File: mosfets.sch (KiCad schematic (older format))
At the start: 28 parts, among them Q12 PSMN1R2-30YLC,115, Q13 PSMN1R2-30YLC,115, Q14 PSMN1R2-30YLC,115, Q15 IRLML0030TRPbF, Q16 IRLML0030TRPbF, Q17 IRLML0030TRPbF, Q18 IRLML0030TRPbF

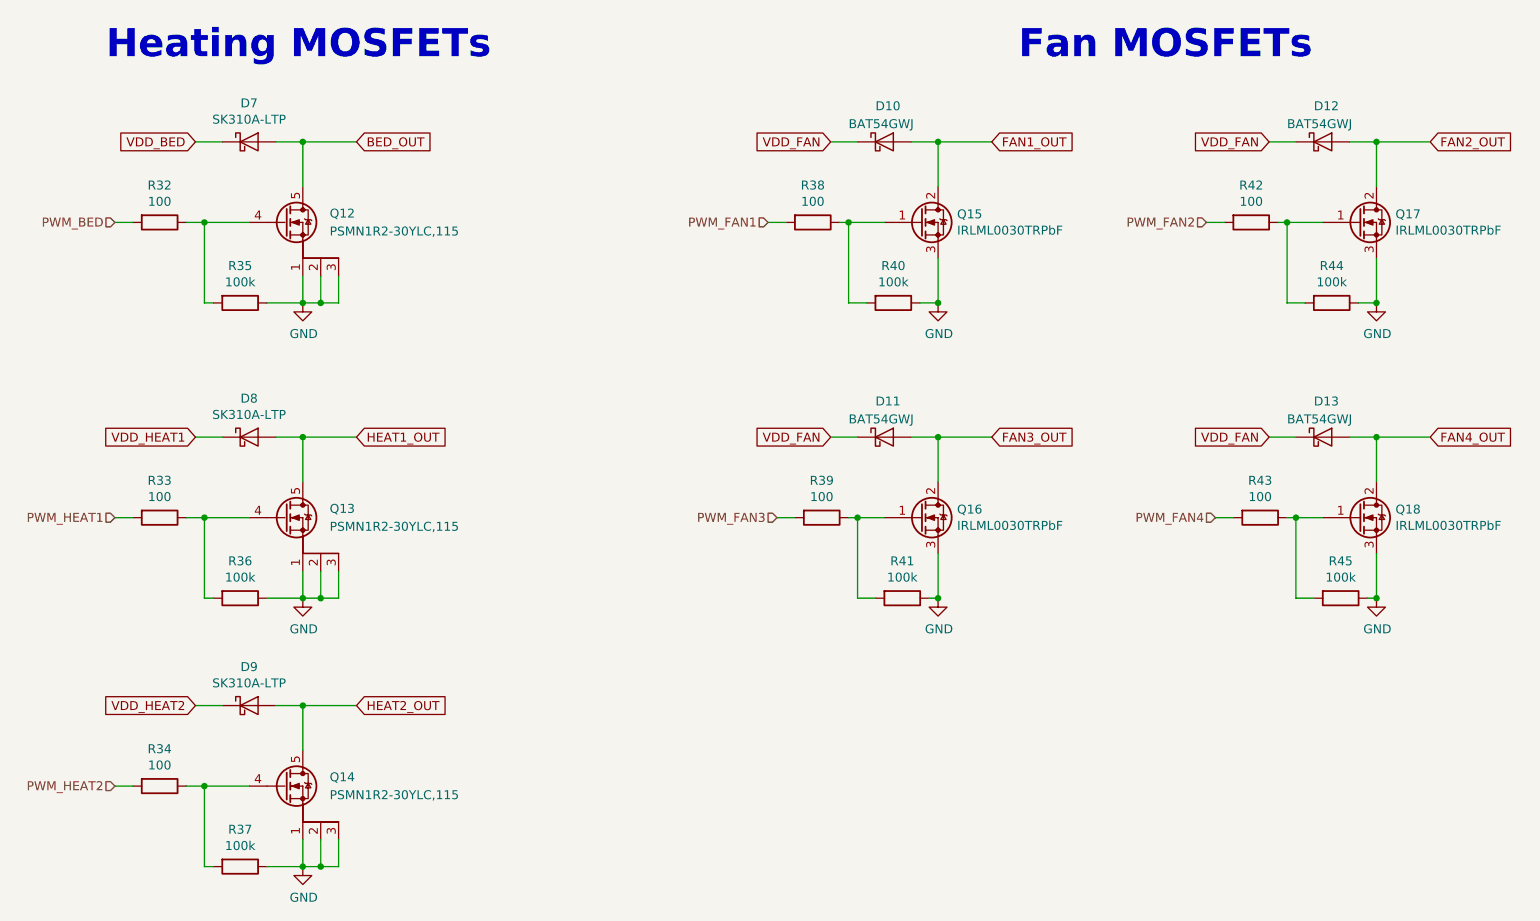
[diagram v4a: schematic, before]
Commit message: Add PD resistor to BOOT PIN
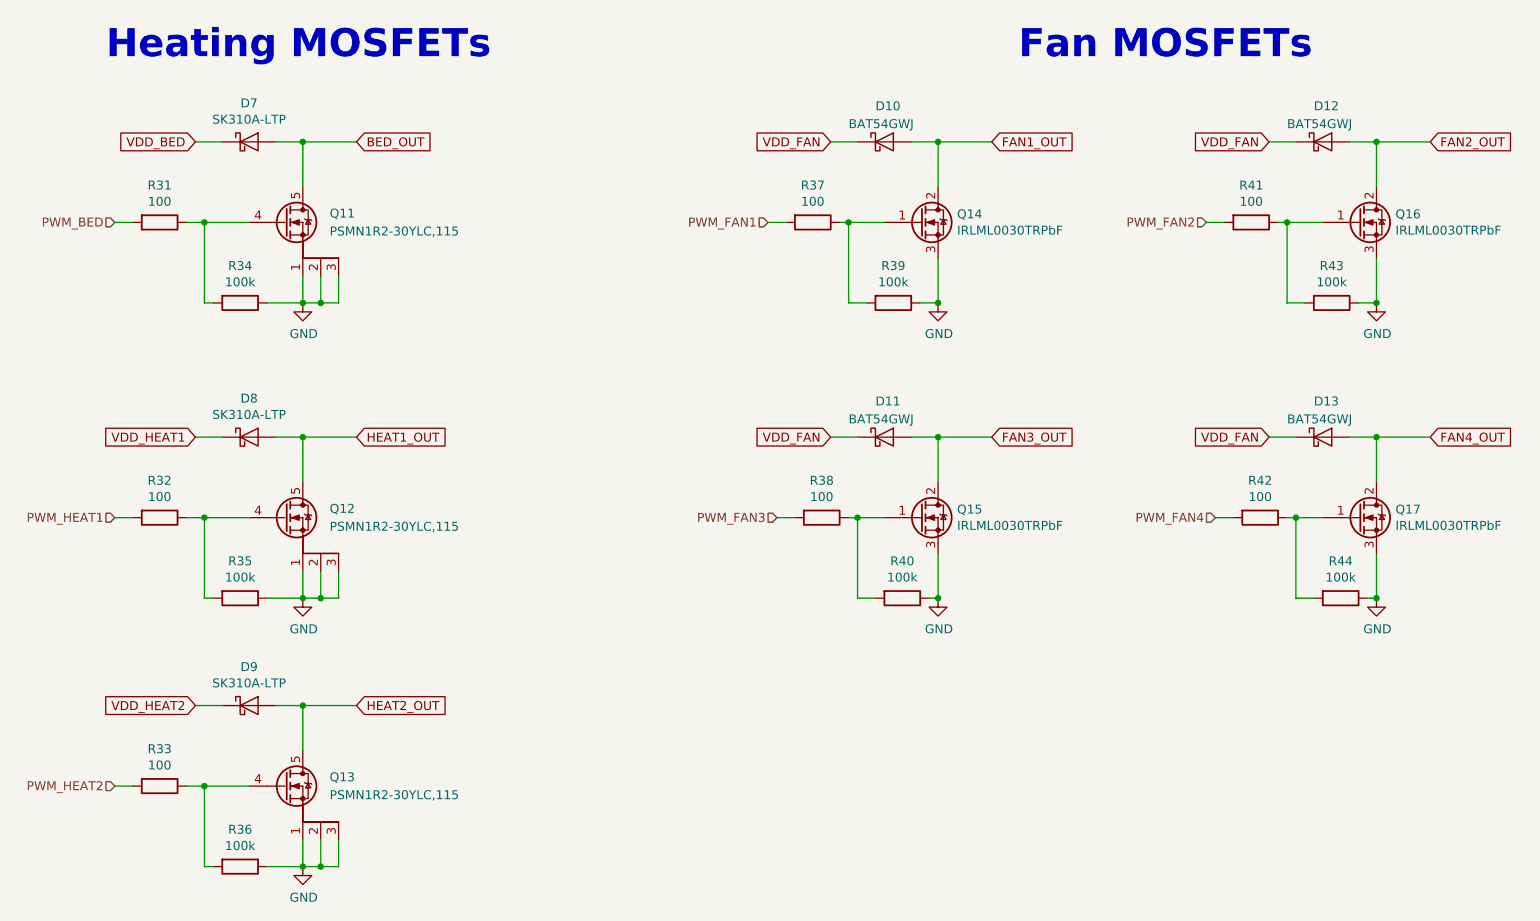
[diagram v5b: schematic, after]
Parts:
- renumbered Q12 to Q11, Q13 to Q12, Q14 to Q13, Q15 to Q14, Q16 to Q15, Q17 to Q16, Q18 to Q17, R32 to R31, R33 to R32, R34 to R33, R35 to R34, R36 to R35, R37 to R36, R38 to R37, R39 to R38, R40 to R39, R41 to R40, R42 to R41, R43 to R42, R44 to R43, R45 to R44
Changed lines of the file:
@@
 EESchema Schematic File Version 4
 LIBS:heteromycin-cache
-EELAYER 29 0
+EELAYER 26 0
 EELAYER END
 $Descr A4 11693 8268
@@
 	1700 1300 1850 1300
 $Comp
-L heteromycin:PSMN1R8-40YLC,115 Q12
+L heteromycin:PSMN1R8-40YLC,115 Q11
 U 1 1 5B1A764D
 P 2200 1750
-F 0 "Q12" H 2450 1800 50  0000 L CNN
+F 0 "Q11" H 2450 1800 50  0000 L CNN
 F 1 "PSMN1R2-30YLC,115" H 2450 1700 50  0000 L CNN
 F 2 "heteromycin:SOT-669_LFPAK_ThermalVias-1" H 2400 1675 50  0001 L CIN
@@
 PWM_HEAT1
 $Comp
-L Device:R R32
+L Device:R R31
 U 1 1 5B1AEA5D
 P 1500 1750
-F 0 "R32" V 1293 1750 50  0000 C CNN
+F 0 "R31" V 1293 1750 50  0000 C CNN
 F 1 "100" V 1384 1750 50  0000 C CNN
 F 2 "Resistor_SMD:R_0603_1608Metric" V 1430 1750 50  0001 C CNN
@@
 	2300 3850 2300 3700
 $Comp
-L Device:R R33
+L Device:R R32
 U 1 1 5B1B03DE
 P 1500 3400
-F 0 "R33" V 1293 3400 50  0000 C CNN
+F 0 "R32" V 1293 3400 50  0000 C CNN
 F 1 "100" V 1384 3400 50  0000 C CNN
 F 2 "Resistor_SMD:R_0603_1608Metric" V 1430 3400 50  0001 C CNN
@@
 Connection ~ 2300 2950
 $Comp
-L Device:R R38
+L Device:R R37
 U 1 1 5B1FB287
 P 5150 1750
-F 0 "R38" V 4943 1750 50  0000 C CNN
+F 0 "R37" V 4943 1750 50  0000 C CNN
 F 1 "100" V 5034 1750 50  0000 C CNN
 F 2 "Resistor_SMD:R_0603_1608Metric" V 5080 1750 50  0001 C CNN
@@
 	5850 1950 5850 2200
 $Comp
-L Device:R R39
+L Device:R R38
 U 1 1 5B2008D0
 P 5200 3400
-F 0 "R39" V 4993 3400 50  0000 C CNN
+F 0 "R38" V 4993 3400 50  0000 C CNN
 F 1 "100" V 5084 3400 50  0000 C CNN
 F 2 "Resistor_SMD:R_0603_1608Metric" V 5130 3400 50  0001 C CNN
@@
 	5350 1750 5550 1750
 $Comp
-L Device:R R35
+L Device:R R34
 U 1 1 5AF82135
 P 1950 2200
-F 0 "R35" V 1743 2200 50  0000 C CNN
+F 0 "R34" V 1743 2200 50  0000 C CNN
 F 1 "100k" V 1834 2200 50  0000 C CNN
 F 2 "Resistor_SMD:R_0603_1608Metric" V 1880 2200 50  0001 C CNN
@@
 Connection ~ 2300 2200
 $Comp
-L Device:R R36
+L Device:R R35
 U 1 1 5AF8339E
 P 1950 3850
-F 0 "R36" V 1743 3850 50  0000 C CNN
+F 0 "R35" V 1743 3850 50  0000 C CNN
 F 1 "100k" V 1834 3850 50  0000 C CNN
 F 2 "Resistor_SMD:R_0603_1608Metric" V 1880 3850 50  0001 C CNN
@@
 	2300 3850 2100 3850
 $Comp
-L Device:R R40
+L Device:R R39
 U 1 1 5AF83BB4
 P 5600 2200
-F 0 "R40" V 5393 2200 50  0000 C CNN
+F 0 "R39" V 5393 2200 50  0000 C CNN
 F 1 "100k" V 5484 2200 50  0000 C CNN
 F 2 "Resistor_SMD:R_0603_1608Metric" V 5530 2200 50  0001 C CNN
@@
 Connection ~ 5350 1750
 $Comp
-L Device:R R41
+L Device:R R40
 U 1 1 5AF880C0
 P 5650 3850
-F 0 "R41" V 5443 3850 50  0000 C CNN
+F 0 "R40" V 5443 3850 50  0000 C CNN
 F 1 "100k" V 5534 3850 50  0000 C CNN
 F 2 "Resistor_SMD:R_0603_1608Metric" V 5580 3850 50  0001 C CNN
@@
 VDD_FAN
 $Comp
-L heteromycin:PSMN1R8-40YLC,115 Q13
+L heteromycin:PSMN1R8-40YLC,115 Q12
 U 1 1 5BC30682
 P 2200 3400
-F 0 "Q13" H 2450 3450 50  0000 L CNN
+F 0 "Q12" H 2450 3450 50  0000 L CNN
 F 1 "PSMN1R2-30YLC,115" H 2450 3350 50  0000 L CNN
 F 2 "heteromycin:SOT-669_LFPAK_ThermalVias-1" H 2400 3325 50  0001 L CIN
@@
 	2300 5350 2300 5200
 $Comp
-L Device:R R34
+L Device:R R33
 U 1 1 5BC4CDF3
 P 1500 4900
-F 0 "R34" V 1293 4900 50  0000 C CNN
+F 0 "R33" V 1293 4900 50  0000 C CNN
 F 1 "100" V 1384 4900 50  0000 C CNN
 F 2 "Resistor_SMD:R_0603_1608Metric" V 1430 4900 50  0001 C CNN
@@
 Connection ~ 2300 4450
 $Comp
-L Device:R R37
+L Device:R R36
 U 1 1 5BC4CE00
 P 1950 5350
-F 0 "R37" V 1743 5350 50  0000 C CNN
+F 0 "R36" V 1743 5350 50  0000 C CNN
 F 1 "100k" V 1834 5350 50  0000 C CNN
 F 2 "Resistor_SMD:R_0603_1608Metric" V 1880 5350 50  0001 C CNN
@@
 	2300 5350 2100 5350
 $Comp
-L heteromycin:PSMN1R8-40YLC,115 Q14
+L heteromycin:PSMN1R8-40YLC,115 Q13
 U 1 1 5BC4CE0B
 P 2200 4900
-F 0 "Q14" H 2450 4950 50  0000 L CNN
+F 0 "Q13" H 2450 4950 50  0000 L CNN
 F 1 "PSMN1R2-30YLC,115" H 2450 4850 50  0000 L CNN
 F 2 "heteromycin:SOT-669_LFPAK_ThermalVias-1" H 2400 4825 50  0001 L CIN
@@
 $EndComp
 $Comp
-L Device:R R42
+L Device:R R41
 U 1 1 5BC57CD1
 P 7600 1750
-F 0 "R42" V 7393 1750 50  0000 C CNN
+F 0 "R41" V 7393 1750 50  0000 C CNN
 F 1 "100" V 7484 1750 50  0000 C CNN
 F 2 "Resistor_SMD:R_0603_1608Metric" V 7530 1750 50  0001 C CNN
@@
 	8300 1950 8300 2200
 $Comp
-L Device:R R43
+L Device:R R42
 U 1 1 5BC57CE1
 P 7650 3400
-F 0 "R43" V 7443 3400 50  0000 C CNN
+F 0 "R42" V 7443 3400 50  0000 C CNN
 F 1 "100" V 7534 3400 50  0000 C CNN
 F 2 "Resistor_SMD:R_0603_1608Metric" V 7580 3400 50  0001 C CNN
@@
 	7800 1750 8000 1750
 $Comp
-L Device:R R44
+L Device:R R43
 U 1 1 5BC57CF2
 P 8050 2200
-F 0 "R44" V 7843 2200 50  0000 C CNN
+F 0 "R43" V 7843 2200 50  0000 C CNN
 F 1 "100k" V 7934 2200 50  0000 C CNN
 F 2 "Resistor_SMD:R_0603_1608Metric" V 7980 2200 50  0001 C CNN
@@
 Connection ~ 7800 1750
 $Comp
-L Device:R R45
+L Device:R R44
 U 1 1 5BC57CFF
 P 8100 3850
-F 0 "R45" V 7893 3850 50  0000 C CNN
+F 0 "R44" V 7893 3850 50  0000 C CNN
 F 1 "100k" V 7984 3850 50  0000 C CNN
 F 2 "Resistor_SMD:R_0603_1608Metric" V 8030 3850 50  0001 C CNN
@@
 AR Path="/5BC77F87/5BFEEB5C" Ref="Q?"  Part="1"
 AR Path="/5BC77F8D/5BFEEB5C" Ref="Q?"  Part="1"
-AR Path="/5BC2F648/5BFEEB5C" Ref="Q15"  Part="1"
-F 0 "Q15" H 5956 1796 50  0000 L CNN
+AR Path="/5BC2F648/5BFEEB5C" Ref="Q14"  Part="1"
+F 0 "Q14" H 5956 1796 50  0000 L CNN
 F 1 "IRLML0030TRPbF" H 5956 1705 50  0000 L CNN
 F 2 "Package_TO_SOT_SMD:SOT-23" H 5950 1850 50  0001 C CNN
@@
 AR Path="/5BC77F87/5C004C12" Ref="Q?"  Part="1"
 AR Path="/5BC77F8D/5C004C12" Ref="Q?"  Part="1"
-AR Path="/5BC2F648/5C004C12" Ref="Q16"  Part="1"
-F 0 "Q16" H 5956 3446 50  0000 L CNN
+AR Path="/5BC2F648/5C004C12" Ref="Q15"  Part="1"
+F 0 "Q15" H 5956 3446 50  0000 L CNN
 F 1 "IRLML0030TRPbF" H 5956 3355 50  0000 L CNN
 F 2 "Package_TO_SOT_SMD:SOT-23" H 5950 3500 50  0001 C CNN
@@
 AR Path="/5BC77F87/5C006AFD" Ref="Q?"  Part="1"
 AR Path="/5BC77F8D/5C006AFD" Ref="Q?"  Part="1"
-AR Path="/5BC2F648/5C006AFD" Ref="Q17"  Part="1"
-F 0 "Q17" H 8406 1796 50  0000 L CNN
+AR Path="/5BC2F648/5C006AFD" Ref="Q16"  Part="1"
+F 0 "Q16" H 8406 1796 50  0000 L CNN
 F 1 "IRLML0030TRPbF" H 8406 1705 50  0000 L CNN
 F 2 "Package_TO_SOT_SMD:SOT-23" H 8400 1850 50  0001 C CNN
@@
 AR Path="/5BC77F87/5C0089E5" Ref="Q?"  Part="1"
 AR Path="/5BC77F8D/5C0089E5" Ref="Q?"  Part="1"
-AR Path="/5BC2F648/5C0089E5" Ref="Q18"  Part="1"
-F 0 "Q18" H 8406 3446 50  0000 L CNN
+AR Path="/5BC2F648/5C0089E5" Ref="Q17"  Part="1"
+F 0 "Q17" H 8406 3446 50  0000 L CNN
 F 1 "IRLML0030TRPbF" H 8406 3355 50  0000 L CNN
 F 2 "Package_TO_SOT_SMD:SOT-23" H 8400 3500 50  0001 C CNN
